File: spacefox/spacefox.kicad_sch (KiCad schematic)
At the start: 7 parts, among them U1 ProMicro

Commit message: WIP V2 PCB
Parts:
- added H1, H2, H3, H4: MountingHole, MountingHole:MountingHole_3.2mm_M3, symbol Mechanical:MountingHole
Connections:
- net at RV1.2: now also U1.18 (F6); no longer U1.9 (D7)
- net at U1.11 (B4): no longer RV2.2
- net at U1.12 (B5): now also RV4.2; no longer RV5.2
- net at U1.13 (B6): now also RV6.2
- net at U1.17 (F7): now also RV3.2
- net at U1.19 (F5): now also RV5.2; no longer RV4.2
- net at U1.20 (F4): now also RV2.2; no longer RV3.2
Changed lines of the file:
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@@
     (stroke (width 0) (type default) (color 0 0 0 0))
   )
-  (wire (pts (xy 114.3 114.3) (xy 114.3 96.52))
-    (stroke (width 0) (type default) (color 0 0 0 0))
-  )
-  (wire (pts (xy 161.29 78.74) (xy 149.86 78.74))
-    (stroke (width 0) (type default) (color 0 0 0 0))
-  )
-  (wire (pts (xy 205.74 119.38) (xy 205.74 81.28))
-    (stroke (width 0) (type default) (color 0 0 0 0))
-  )
-  (wire (pts (xy 149.86 81.28) (xy 205.74 81.28))
-    (stroke (width 0) (type default) (color 0 0 0 0))
-  )
-  (wire (pts (xy 96.52 113.03) (xy 100.33 113.03))
+  (wire (pts (xy 172.72 86.36) (xy 149.86 86.36))
+    (stroke (width 0) (type default) (color 0 0 0 0))
+  )
+  (wire (pts (xy 167.64 39.37) (xy 167.64 83.82))
+    (stroke (width 0) (type default) (color 0 0 0 0))
+  )
+  (wire (pts (xy 186.69 115.57) (xy 114.3 115.57))
+    (stroke (width 0) (type default) (color 0 0 0 0))
+  )
+  (wire (pts (xy 149.86 81.28) (xy 170.18 81.28))
     (stroke (width 0) (type default) (color 0 0 0 0))
   )
@@
     (stroke (width 0) (type default) (color 0 0 0 0))
   )
-  (wire (pts (xy 100.33 113.03) (xy 100.33 93.98))
+  (wire (pts (xy 166.37 78.74) (xy 149.86 78.74))
+    (stroke (width 0) (type default) (color 0 0 0 0))
+  )
+  (wire (pts (xy 167.64 83.82) (xy 149.86 83.82))
+    (stroke (width 0) (type default) (color 0 0 0 0))
+  )
+  (wire (pts (xy 96.52 113.03) (xy 166.37 113.03))
     (stroke (width 0) (type default) (color 0 0 0 0))
   )
@@
     (stroke (width 0) (type default) (color 0 0 0 0))
   )
-  (wire (pts (xy 149.86 83.82) (xy 181.61 83.82))
-    (stroke (width 0) (type default) (color 0 0 0 0))
-  )
-  (wire (pts (xy 181.61 137.16) (xy 181.61 83.82))
-    (stroke (width 0) (type default) (color 0 0 0 0))
-  )
-  (wire (pts (xy 118.11 135.89) (xy 118.11 114.3))
+  (wire (pts (xy 186.69 132.08) (xy 186.69 115.57))
     (stroke (width 0) (type default) (color 0 0 0 0))
   )
@@
     (stroke (width 0) (type default) (color 0 0 0 0))
   )
-  (wire (pts (xy 118.11 114.3) (xy 114.3 114.3))
-    (stroke (width 0) (type default) (color 0 0 0 0))
-  )
-  (wire (pts (xy 161.29 34.29) (xy 151.13 34.29))
-    (stroke (width 0) (type default) (color 0 0 0 0))
-  )
-  (wire (pts (xy 161.29 34.29) (xy 161.29 78.74))
-    (stroke (width 0) (type default) (color 0 0 0 0))
-  )
-  (wire (pts (xy 110.49 88.9) (xy 114.3 88.9))
-    (stroke (width 0) (type default) (color 0 0 0 0))
-  )
-  (wire (pts (xy 100.33 93.98) (xy 114.3 93.98))
+  (wire (pts (xy 181.61 96.52) (xy 149.86 96.52))
+    (stroke (width 0) (type default) (color 0 0 0 0))
+  )
+  (wire (pts (xy 118.11 135.89) (xy 170.18 135.89))
+    (stroke (width 0) (type default) (color 0 0 0 0))
+  )
+  (wire (pts (xy 205.74 132.08) (xy 186.69 132.08))
+    (stroke (width 0) (type default) (color 0 0 0 0))
+  )
+  (wire (pts (xy 110.49 39.37) (xy 167.64 39.37))
+    (stroke (width 0) (type default) (color 0 0 0 0))
+  )
+  (wire (pts (xy 181.61 137.16) (xy 181.61 96.52))
+    (stroke (width 0) (type default) (color 0 0 0 0))
+  )
+  (wire (pts (xy 151.13 34.29) (xy 172.72 34.29))
+    (stroke (width 0) (type default) (color 0 0 0 0))
+  )
+  (wire (pts (xy 114.3 115.57) (xy 114.3 96.52))
+    (stroke (width 0) (type default) (color 0 0 0 0))
+  )
+  (wire (pts (xy 205.74 119.38) (xy 205.74 132.08))
+    (stroke (width 0) (type default) (color 0 0 0 0))
+  )
+  (wire (pts (xy 170.18 135.89) (xy 170.18 81.28))
+    (stroke (width 0) (type default) (color 0 0 0 0))
+  )
+  (wire (pts (xy 172.72 34.29) (xy 172.72 86.36))
     (stroke (width 0) (type default) (color 0 0 0 0))
   )
@@
     (stroke (width 0) (type default) (color 0 0 0 0))
   )
+  (wire (pts (xy 166.37 78.74) (xy 166.37 113.03))
+    (stroke (width 0) (type default) (color 0 0 0 0))
+  )
   (wire (pts (xy 114.3 73.66) (xy 109.22 73.66))
-    (stroke (width 0) (type default) (color 0 0 0 0))
-  )
-  (wire (pts (xy 110.49 39.37) (xy 110.49 88.9))
     (stroke (width 0) (type default) (color 0 0 0 0))
   )
@@
     (pin "3")
   )
+  (symbol (lib_id "Mechanical:MountingHole") (at 210.82 173.99 0) (unit 1)
+    (in_bom yes) (on_board yes) (fields_autoplaced)
+    (property "Reference" "H2" (id 0) (at 213.36 172.7199 0)
+      (effects (font (size 1.27 1.27)) (justify left))
+    )
+    (property "Value" "MountingHole" (id 1) (at 213.36 175.2599 0)
+      (effects (font (size 1.27 1.27)) (justify left))
+    )
+    (property "Footprint" "MountingHole:MountingHole_3.2mm_M3" (id 2) (at 210.82 173.99 0)
+      (effects (font (size 1.27 1.27)) hide)
+    )
+    (property "Datasheet" "~" (id 3) (at 210.82 173.99 0)
+      (effects (font (size 1.27 1.27)) hide)
+    )
+  )
+  (symbol (lib_id "Mechanical:MountingHole") (at 259.08 171.45 0) (unit 1)
+    (in_bom yes) (on_board yes) (fields_autoplaced)
+    (property "Reference" "H4" (id 0) (at 261.62 170.1799 0)
+      (effects (font (size 1.27 1.27)) (justify left))
+    )
+    (property "Value" "MountingHole" (id 1) (at 261.62 172.7199 0)
+      (effects (font (size 1.27 1.27)) (justify left))
+    )
+    (property "Footprint" "MountingHole:MountingHole_3.2mm_M3" (id 2) (at 259.08 171.45 0)
+      (effects (font (size 1.27 1.27)) hide)
+    )
+    (property "Datasheet" "~" (id 3) (at 259.08 171.45 0)
+      (effects (font (size 1.27 1.27)) hide)
+    )
+  )
   (symbol (lib_id "power:GND") (at 201.93 123.19 0) (unit 1)
     (in_bom yes) (on_board yes) (fields_autoplaced)
@@
     (pin "1")
   )
+  (symbol (lib_id "Mechanical:MountingHole") (at 234.95 171.45 0) (unit 1)
+    (in_bom yes) (on_board yes) (fields_autoplaced)
+    (property "Reference" "H3" (id 0) (at 237.49 170.1799 0)
+      (effects (font (size 1.27 1.27)) (justify left))
+    )
+    (property "Value" "MountingHole" (id 1) (at 237.49 172.7199 0)
+      (effects (font (size 1.27 1.27)) (justify left))
+    )
+    (property "Footprint" "MountingHole:MountingHole_3.2mm_M3" (id 2) (at 234.95 171.45 0)
+      (effects (font (size 1.27 1.27)) hide)
+    )
+    (property "Datasheet" "~" (id 3) (at 234.95 171.45 0)
+      (effects (font (size 1.27 1.27)) hide)
+    )
+  )
   (symbol (lib_id "Device:R_Potentiometer") (at 177.8 137.16 0) (unit 1)
     (in_bom yes) (on_board yes) (fields_autoplaced)
@@
     )
     (pin "1")
+  )
+  (symbol (lib_id "Mechanical:MountingHole") (at 186.69 172.72 0) (unit 1)
+    (in_bom yes) (on_board yes) (fields_autoplaced)
+    (property "Reference" "H1" (id 0) (at 189.23 171.4499 0)
+      (effects (font (size 1.27 1.27)) (justify left))
+    )
+    (property "Value" "MountingHole" (id 1) (at 189.23 173.9899 0)
+      (effects (font (size 1.27 1.27)) (justify left))
+    )
+    (property "Footprint" "MountingHole:MountingHole_3.2mm_M3" (id 2) (at 186.69 172.72 0)
+      (effects (font (size 1.27 1.27)) hide)
+    )
+    (property "Datasheet" "~" (id 3) (at 186.69 172.72 0)
+      (effects (font (size 1.27 1.27)) hide)
+    )
   )
   (symbol (lib_id "power:VCC") (at 147.32 30.48 0) (unit 1)
@@
       (reference "#PWR0115") (unit 1) (value "VCC") (footprint "")
     )
+    (path "/d297dbe3-8fda-4cb5-b9a2-9046bf02d7c7"
+      (reference "H1") (unit 1) (value "MountingHole") (footprint "MountingHole:MountingHole_3.2mm_M3")
+    )
+    (path "/798de0fc-3a61-40f2-993d-774cb895b4c4"
+      (reference "H2") (unit 1) (value "MountingHole") (footprint "MountingHole:MountingHole_3.2mm_M3")
+    )
+    (path "/b298bbb0-7dc9-41c0-b303-e42cf6c758d3"
+      (reference "H3") (unit 1) (value "MountingHole") (footprint "MountingHole:MountingHole_3.2mm_M3")
+    )
+    (path "/7bf014b8-59a7-4274-bba0-e4c0e27ac1d7"
+      (reference "H4") (unit 1) (value "MountingHole") (footprint "MountingHole:MountingHole_3.2mm_M3")
+    )
     (path "/4f742341-3ea4-44a1-a430-a2f5991a393f"

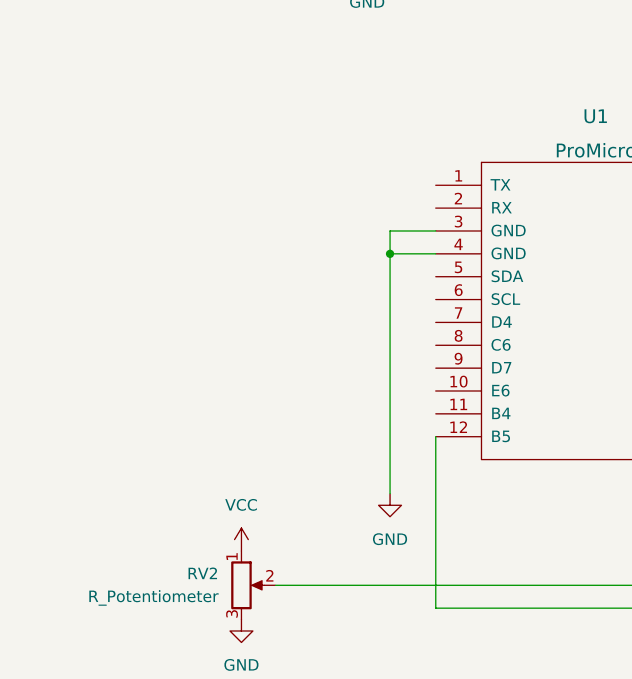
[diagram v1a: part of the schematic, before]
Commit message: update top knob
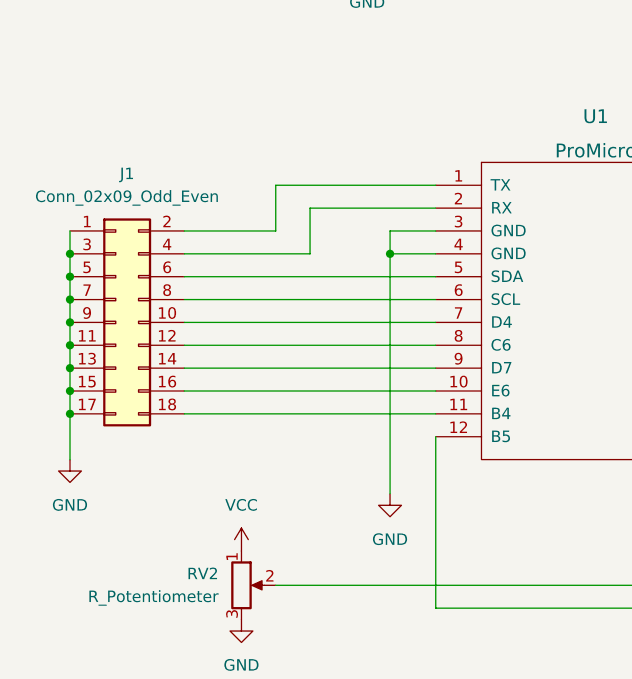
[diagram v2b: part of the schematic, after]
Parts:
- added J1: Conn_02x09_Odd_Even, Connector_PinHeader_2.54mm:PinHeader_2x09_P2.54mm_Vertical, symbol Connector_Generic:Conn_02x09_Odd_Even
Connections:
- net GND: now also J1.1 (Pin_1), J1.11 (Pin_11), J1.13 (Pin_13), J1.15 (Pin_15), J1.17 (Pin_17), J1.3 (Pin_3), J1.5 (Pin_5), J1.7 (Pin_7), J1.9 (Pin_9)
- net at U1.1 (TX): now also J1.2 (Pin_2)
- net at U1.10 (E6): now also J1.16 (Pin_16)
- net at U1.11 (B4): now also J1.18 (Pin_18)
- net at U1.2 (RX): now also J1.4 (Pin_4)
- net at U1.5 (SDA): now also J1.6 (Pin_6)
- net at U1.6 (SCL): now also J1.8 (Pin_8)
- net at U1.7 (D4): now also J1.10 (Pin_10)
- net at U1.8 (C6): now also J1.12 (Pin_12)
- net at U1.9 (D7): now also J1.14 (Pin_14)
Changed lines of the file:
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@@
 (kicad_sch (version 20211123) (generator eeschema)
   (paper "A4")
+  (junction (at 73.66 78.74) (diameter 0) (color 0 0 0 0)
+  )
+  (junction (at 73.66 86.36) (diameter 0) (color 0 0 0 0)
+  )
+  (junction (at 73.66 76.2) (diameter 0) (color 0 0 0 0)
+  )
+  (junction (at 73.66 88.9) (diameter 0) (color 0 0 0 0)
+  )
   (junction (at 109.22 76.2) (diameter 0) (color 0 0 0 0)
   )
+  (junction (at 73.66 81.28) (diameter 0) (color 0 0 0 0)
+  )
+  (junction (at 73.66 83.82) (diameter 0) (color 0 0 0 0)
+  )
+  (junction (at 73.66 93.98) (diameter 0) (color 0 0 0 0)
+  )
+  (junction (at 73.66 91.44) (diameter 0) (color 0 0 0 0)
+  )
   (wire (pts (xy 158.75 76.2) (xy 158.75 62.23))
     (stroke (width 0) (type default) (color 0 0 0 0))
   )
+  (wire (pts (xy 73.66 83.82) (xy 73.66 86.36))
+    (stroke (width 0) (type default) (color 0 0 0 0))
+  )
   (wire (pts (xy 172.72 86.36) (xy 149.86 86.36))
     (stroke (width 0) (type default) (color 0 0 0 0))
   )
+  (wire (pts (xy 73.66 91.44) (xy 73.66 93.98))
+    (stroke (width 0) (type default) (color 0 0 0 0))
+  )
+  (wire (pts (xy 73.66 88.9) (xy 73.66 91.44))
+    (stroke (width 0) (type default) (color 0 0 0 0))
+  )
   (wire (pts (xy 167.64 39.37) (xy 167.64 83.82))
     (stroke (width 0) (type default) (color 0 0 0 0))
   )
+  (wire (pts (xy 73.66 86.36) (xy 73.66 88.9))
+    (stroke (width 0) (type default) (color 0 0 0 0))
+  )
   (wire (pts (xy 186.69 115.57) (xy 114.3 115.57))
     (stroke (width 0) (type default) (color 0 0 0 0))
@@
     (stroke (width 0) (type default) (color 0 0 0 0))
   )
+  (wire (pts (xy 86.36 76.2) (xy 100.33 76.2))
+    (stroke (width 0) (type default) (color 0 0 0 0))
+  )
   (wire (pts (xy 96.52 113.03) (xy 166.37 113.03))
     (stroke (width 0) (type default) (color 0 0 0 0))
   )
+  (wire (pts (xy 86.36 91.44) (xy 114.3 91.44))
+    (stroke (width 0) (type default) (color 0 0 0 0))
+  )
   (wire (pts (xy 109.22 76.2) (xy 114.3 76.2))
     (stroke (width 0) (type default) (color 0 0 0 0))
@@
     (stroke (width 0) (type default) (color 0 0 0 0))
   )
+  (wire (pts (xy 86.36 81.28) (xy 114.3 81.28))
+    (stroke (width 0) (type default) (color 0 0 0 0))
+  )
+  (wire (pts (xy 86.36 78.74) (xy 114.3 78.74))
+    (stroke (width 0) (type default) (color 0 0 0 0))
+  )
+  (wire (pts (xy 73.66 93.98) (xy 73.66 99.06))
+    (stroke (width 0) (type default) (color 0 0 0 0))
+  )
   (wire (pts (xy 186.69 132.08) (xy 186.69 115.57))
     (stroke (width 0) (type default) (color 0 0 0 0))
   )
+  (wire (pts (xy 100.33 71.12) (xy 114.3 71.12))
+    (stroke (width 0) (type default) (color 0 0 0 0))
+  )
   (wire (pts (xy 149.86 76.2) (xy 158.75 76.2))
     (stroke (width 0) (type default) (color 0 0 0 0))
   )
+  (wire (pts (xy 96.52 68.58) (xy 96.52 73.66))
+    (stroke (width 0) (type default) (color 0 0 0 0))
+  )
+  (wire (pts (xy 86.36 93.98) (xy 114.3 93.98))
+    (stroke (width 0) (type default) (color 0 0 0 0))
+  )
   (wire (pts (xy 181.61 96.52) (xy 149.86 96.52))
     (stroke (width 0) (type default) (color 0 0 0 0))
   )
+  (wire (pts (xy 114.3 68.58) (xy 96.52 68.58))
+    (stroke (width 0) (type default) (color 0 0 0 0))
+  )
   (wire (pts (xy 118.11 135.89) (xy 170.18 135.89))
     (stroke (width 0) (type default) (color 0 0 0 0))
   )
+  (wire (pts (xy 73.66 73.66) (xy 73.66 76.2))
+    (stroke (width 0) (type default) (color 0 0 0 0))
+  )
   (wire (pts (xy 205.74 132.08) (xy 186.69 132.08))
     (stroke (width 0) (type default) (color 0 0 0 0))
@@
     (stroke (width 0) (type default) (color 0 0 0 0))
   )
+  (wire (pts (xy 73.66 78.74) (xy 73.66 81.28))
+    (stroke (width 0) (type default) (color 0 0 0 0))
+  )
   (wire (pts (xy 181.61 137.16) (xy 181.61 96.52))
     (stroke (width 0) (type default) (color 0 0 0 0))
   )
+  (wire (pts (xy 73.66 76.2) (xy 73.66 78.74))
+    (stroke (width 0) (type default) (color 0 0 0 0))
+  )
+  (wire (pts (xy 86.36 86.36) (xy 114.3 86.36))
+    (stroke (width 0) (type default) (color 0 0 0 0))
+  )
   (wire (pts (xy 151.13 34.29) (xy 172.72 34.29))
     (stroke (width 0) (type default) (color 0 0 0 0))
   )
+  (wire (pts (xy 73.66 81.28) (xy 73.66 83.82))
+    (stroke (width 0) (type default) (color 0 0 0 0))
+  )
   (wire (pts (xy 114.3 115.57) (xy 114.3 96.52))
     (stroke (width 0) (type default) (color 0 0 0 0))
@@
     (stroke (width 0) (type default) (color 0 0 0 0))
   )
+  (wire (pts (xy 96.52 73.66) (xy 86.36 73.66))
+    (stroke (width 0) (type default) (color 0 0 0 0))
+  )
   (wire (pts (xy 170.18 135.89) (xy 170.18 81.28))
     (stroke (width 0) (type default) (color 0 0 0 0))
   )
+  (wire (pts (xy 86.36 88.9) (xy 114.3 88.9))
+    (stroke (width 0) (type default) (color 0 0 0 0))
+  )
   (wire (pts (xy 172.72 34.29) (xy 172.72 86.36))
     (stroke (width 0) (type default) (color 0 0 0 0))
@@
     (stroke (width 0) (type default) (color 0 0 0 0))
   )
+  (wire (pts (xy 100.33 76.2) (xy 100.33 71.12))
+    (stroke (width 0) (type default) (color 0 0 0 0))
+  )
   (wire (pts (xy 114.3 73.66) (xy 109.22 73.66))
     (stroke (width 0) (type default) (color 0 0 0 0))
+  )
+  (wire (pts (xy 86.36 83.82) (xy 114.3 83.82))
+    (stroke (width 0) (type default) (color 0 0 0 0))
+  )
+  (symbol (lib_id "power:GND") (at 73.66 99.06 0) (unit 1)
+    (in_bom yes) (on_board yes) (fields_autoplaced)
+    (property "Reference" "#PWR0116" (id 0) (at 73.66 105.41 0)
+      (effects (font (size 1.27 1.27)) hide)
+    )
+    (property "Value" "GND" (id 1) (at 73.66 104.14 0))
+    (property "Footprint" "" (id 2) (at 73.66 99.06 0)
+      (effects (font (size 1.27 1.27)) hide)
+    )
+    (property "Datasheet" "" (id 3) (at 73.66 99.06 0)
+      (effects (font (size 1.27 1.27)) hide)
+    )
+    (pin "1")
   )
   (symbol (lib_id "power:VCC") (at 106.68 35.56 0) (unit 1)
@@
     )
   )
+  (symbol (lib_id "Connector_Generic:Conn_02x09_Odd_Even") (at 78.74 83.82 0) (unit 1)
+    (in_bom yes) (on_board yes) (fields_autoplaced)
+    (property "Reference" "J1" (id 0) (at 80.01 67.31 0))
+    (property "Value" "Conn_02x09_Odd_Even" (id 1) (at 80.01 69.85 0))
+    (property "Footprint" "Connector_PinHeader_2.54mm:PinHeader_2x09_P2.54mm_Vertical" (id 2) (at 78.74 83.82 0)
+      (effects (font (size 1.27 1.27)) hide)
+    )
+    (property "Datasheet" "~" (id 3) (at 78.74 83.82 0)
+      (effects (font (size 1.27 1.27)) hide)
+    )
+    (pin "1")
+    (pin "10")
+    (pin "11")
+    (pin "12")
+    (pin "13")
+    (pin "14")
+    (pin "15")
+    (pin "16")
+    (pin "17")
+    (pin "18")
+    (pin "2")
+    (pin "3")
+    (pin "4")
+    (pin "5")
+    (pin "6")
+    (pin "7")
+    (pin "8")
+    (pin "9")
+  )
   (symbol (lib_id "power:GND") (at 201.93 123.19 0) (unit 1)
     (in_bom yes) (on_board yes) (fields_autoplaced)
@@
       (reference "#PWR0115") (unit 1) (value "VCC") (footprint "")
     )
+    (path "/1fc06bcb-f27f-4e96-82ec-74ac4e858281"
+      (reference "#PWR0116") (unit 1) (value "GND") (footprint "")
+    )
     (path "/d297dbe3-8fda-4cb5-b9a2-9046bf02d7c7"
       (reference "H1") (unit 1) (value "MountingHole") (footprint "MountingHole:MountingHole_3.2mm_M3")
@@
       (reference "H4") (unit 1) (value "MountingHole") (footprint "MountingHole:MountingHole_3.2mm_M3")
     )
+    (path "/8a0bdc86-b6d8-4d77-9eb5-e56f1c76aaa1"
+      (reference "J1") (unit 1) (value "Conn_02x09_Odd_Even") (footprint "Connector_PinHeader_2.54mm:PinHeader_2x09_P2.54mm_Vertical")
+    )
     (path "/4f742341-3ea4-44a1-a430-a2f5991a393f"
